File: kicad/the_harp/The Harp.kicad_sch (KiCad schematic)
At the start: 0 parts

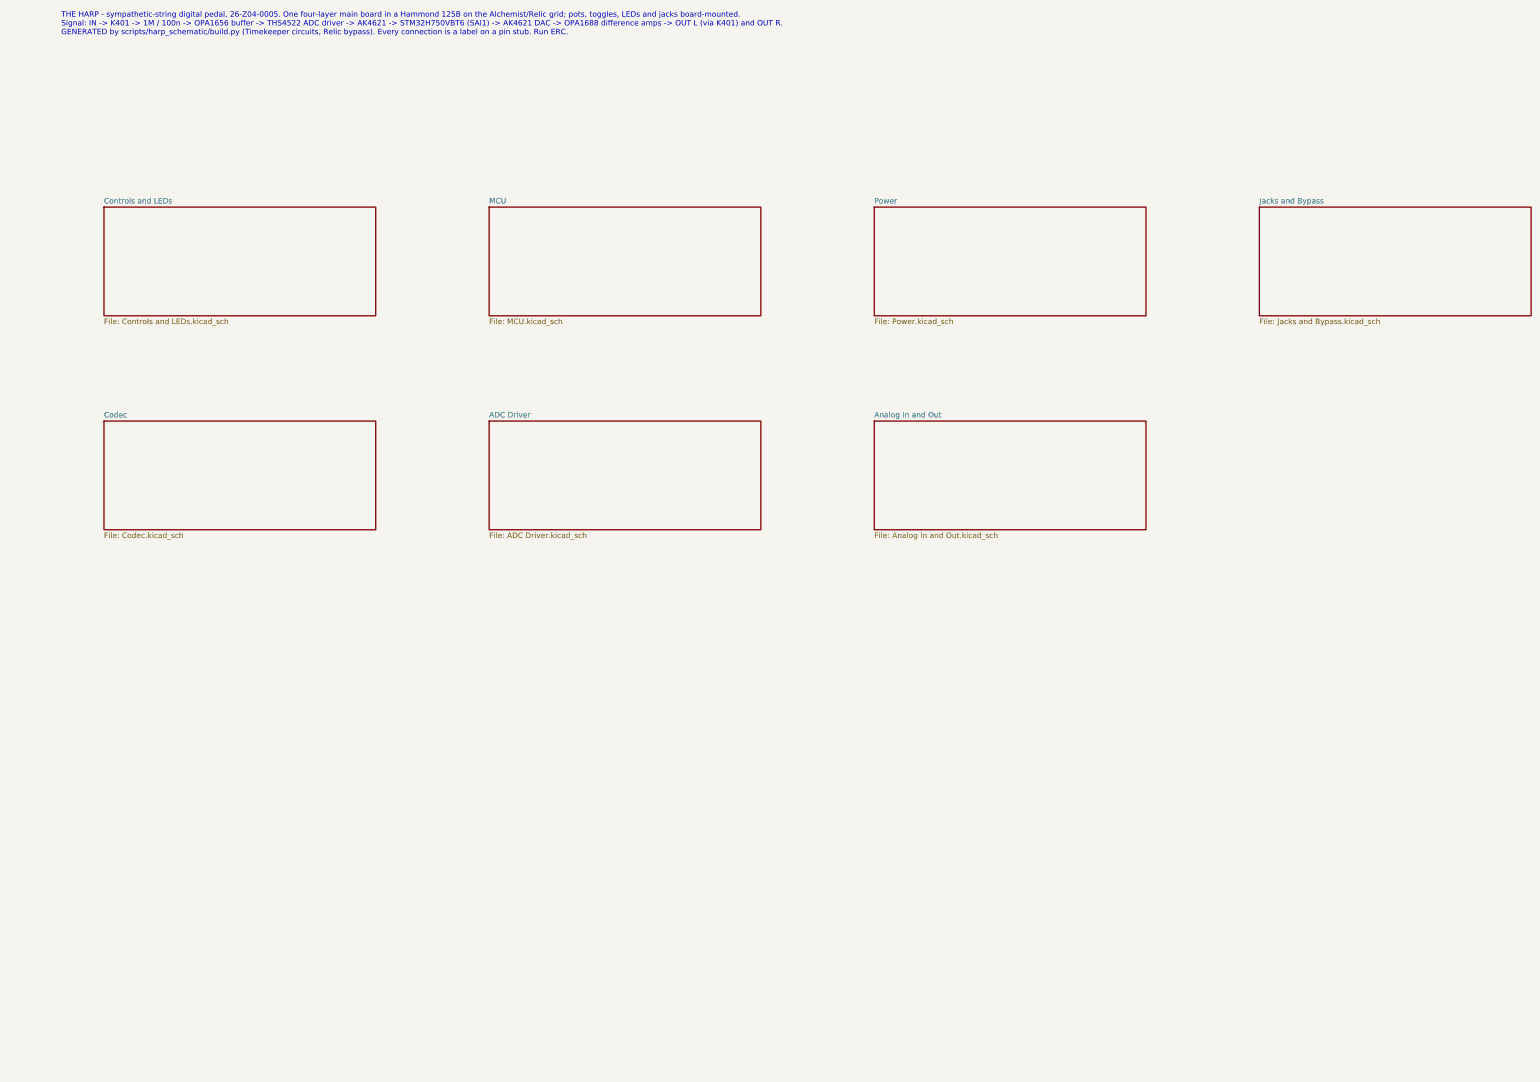
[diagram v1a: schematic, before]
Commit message: Top sheet drawn as a coloured block diagram; embed the title block and Oswald
Sheet blocks coloured by domain inside AUDIO / ANALOG, CONTROL / DIGITAL and
POWER frames, a parts summary in each block, every inter-sheet net as a
coloured arrowed line (drawing only; the sheets connect through global
labels), a legend, and the AW Titleblock 2025 worksheet and Oswald Regular /
Bold embedded as on The Relic's top sheet.

Co-Authored-By: Claude Fable 5.1 <noreply@anthropic.com>
Claude-Session: https://claude.ai/code/session_01TSLeRh1r4phcduukMUZ1ao
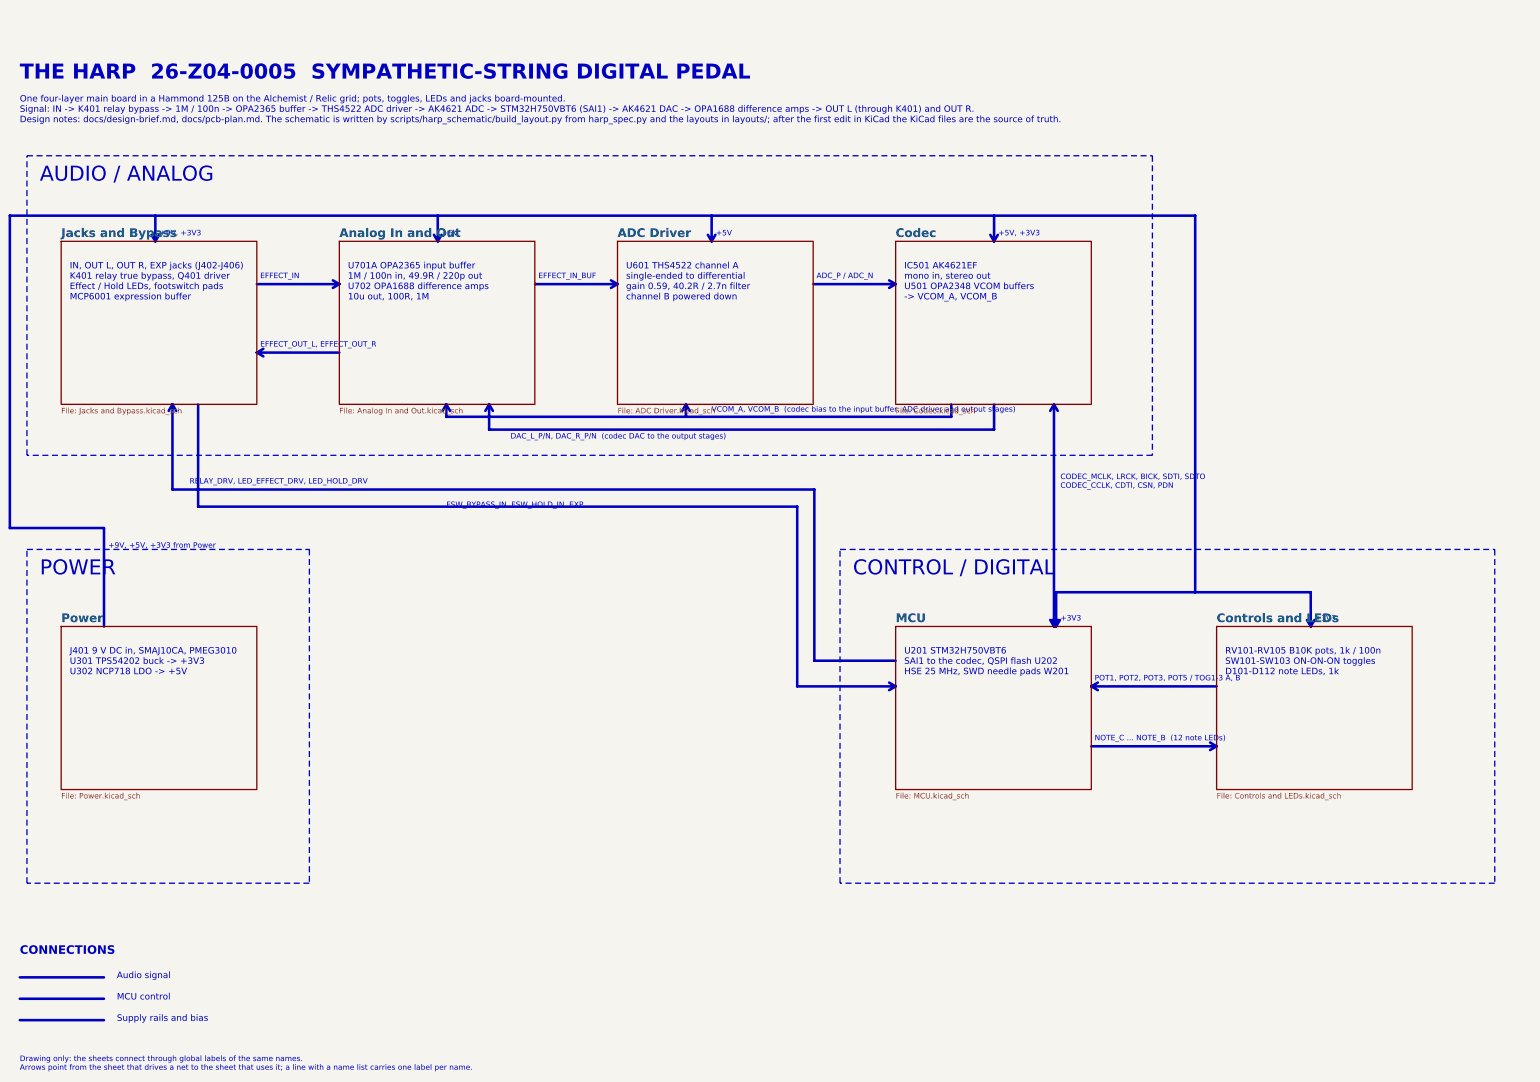
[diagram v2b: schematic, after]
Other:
- note added: "+3V3"
- note added: "+5V"
- note added: "+5V, +3V3"
- note added: "+9V, +3V3"
- note added: "+9V, +5V, +3V3 from Power"
- note added: "ADC_P / ADC_N"
- note added: "AUDIO / ANALOG"
- note added: "Audio signal"
- note added: "CODEC_MCLK, LRCK, BICK, SDTI, SDTO CODEC_CCLK, CDTI, CSN, PDN"
- note added: "CONNECTIONS"
- note added: "CONTROL / DIGITAL"
- note added: "DAC_L_P/N, DAC_R_P/N (codec DAC to the output stages)"
- note added: "Drawing only: the sheets connect through global labels of the same names. Arrows point from the sheet that drives a net to the sheet that uses it; a line with a name list carries one label per name."
- note added: "EFFECT_IN"
- note added: "EFFECT_IN_BUF"
- note added: "EFFECT_OUT_L, EFFECT_OUT_R"
- note added: "FSW_BYPASS_IN, FSW_HOLD_IN, EXP"
- note added: "IC501 AK4621EF mono in, stereo out U501 OPA2348 VCOM buffers -> VCOM_A, VCOM_B"
- note added: "IN, OUT L, OUT R, EXP jacks (J402-J406) K401 relay true bypass, Q401 driver Effect / Hold LEDs, footswitch pads MCP6001 expression buffer"
- note added: "J401 9 V DC in, SMAJ10CA, PMEG3010 U301 TPS54202 buck -> +3V3 U302 NCP718 LDO -> +5V"
- note added: "MCU control"
- note added: "NOTE_C ... NOTE_B (12 note LEDs)"
- note added: "One four-layer main board in a Hammond 125B on the Alchemist / Relic grid; pots, toggles, LEDs and jacks board-mounted. Signal: IN -> K401 relay bypass -> 1M / 100n -> OPA2365 buffer -> THS4522 ADC driver -> AK4621 ADC -> STM32H750VBT6 (SAI1) -> AK4621 DAC -> OPA1688 difference amps -> OUT L (through K401) and OUT R. Design notes: docs/design-brief.md, docs/pcb-plan.md. The schematic is written b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"
- note added: "POT1, POT2, POT3, POT5 / TOG1-3 A, B"
- note added: "POWER"
- note added: "RELAY_DRV, LED_EFFECT_DRV, LED_HOLD_DRV"
- note added: "RV101-RV105 B10K pots, 1k / 100n SW101-SW103 ON-ON-ON toggles D101-D112 note LEDs, 1k"
- note added: "Supply rails and bias"
- note added: "THE HARP 26-Z04-0005 SYMPATHETIC-STRING DIGITAL PEDAL"
- note added: "U201 STM32H750VBT6 SAI1 to the codec, QSPI flash U202 HSE 25 MHz, SWD needle pads W201"
- note added: "U601 THS4522 channel A single-ended to differential gain 0.59, 40.2R / 2.7n filter channel B powered down"
- note added: "U701A OPA2365 input buffer 1M / 100n in, 49.9R / 220p out U702 OPA1688 difference amps 10u out, 100R, 1M"
- note added: "VCOM_A, VCOM_B (codec bias to the input buffer, ADC driver and output stages)"
- note removed: "THE HARP - sympathetic-string digital pedal, 26-Z04-0005. One four-layer main board in a Hammond 125B on the Alchemist/Relic grid; pots, toggles, LEDs and jacks board-mounted. Signal: IN -> K401 -> 1M / 100n -> OPA1656 buffer -> THS4522 ADC driver -> AK4621 -> STM32H750VBT6 (SAI1) -> AK4621 DAC -> OPA1688 difference amps -> OUT L (via K401) and OUT R. GENERATED by scripts/harp_schematic/build.py 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"

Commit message: Stereo single-ended input and an OLED display
IN becomes a TRS jack (tip left, ring right) with a second OPA2365 buffer and
THS4522 channel B into the AK4621EF's AINR; the codec inputs are no longer
parked. A mono plug is detected by the right channel reading silence. The
twelve note LEDs and R107-R118 give way to a 0.91 in I2C OLED connector (J408,
PB6/PB7) with 4.7k pull-ups. Schematic regenerated (190 parts, netlist OK on
all sheets); design brief, PCB plan, firmware requirements and the design
report updated. The PCB still carries the old LED footprints until Update PCB
from Schematic is run in KiCad.

Co-Authored-By: Claude Sonnet 5.5 <noreply@anthropic.com>
Claude-Session: https://claude.ai/code/session_016hDejPHPgG8auBLMyByYZK
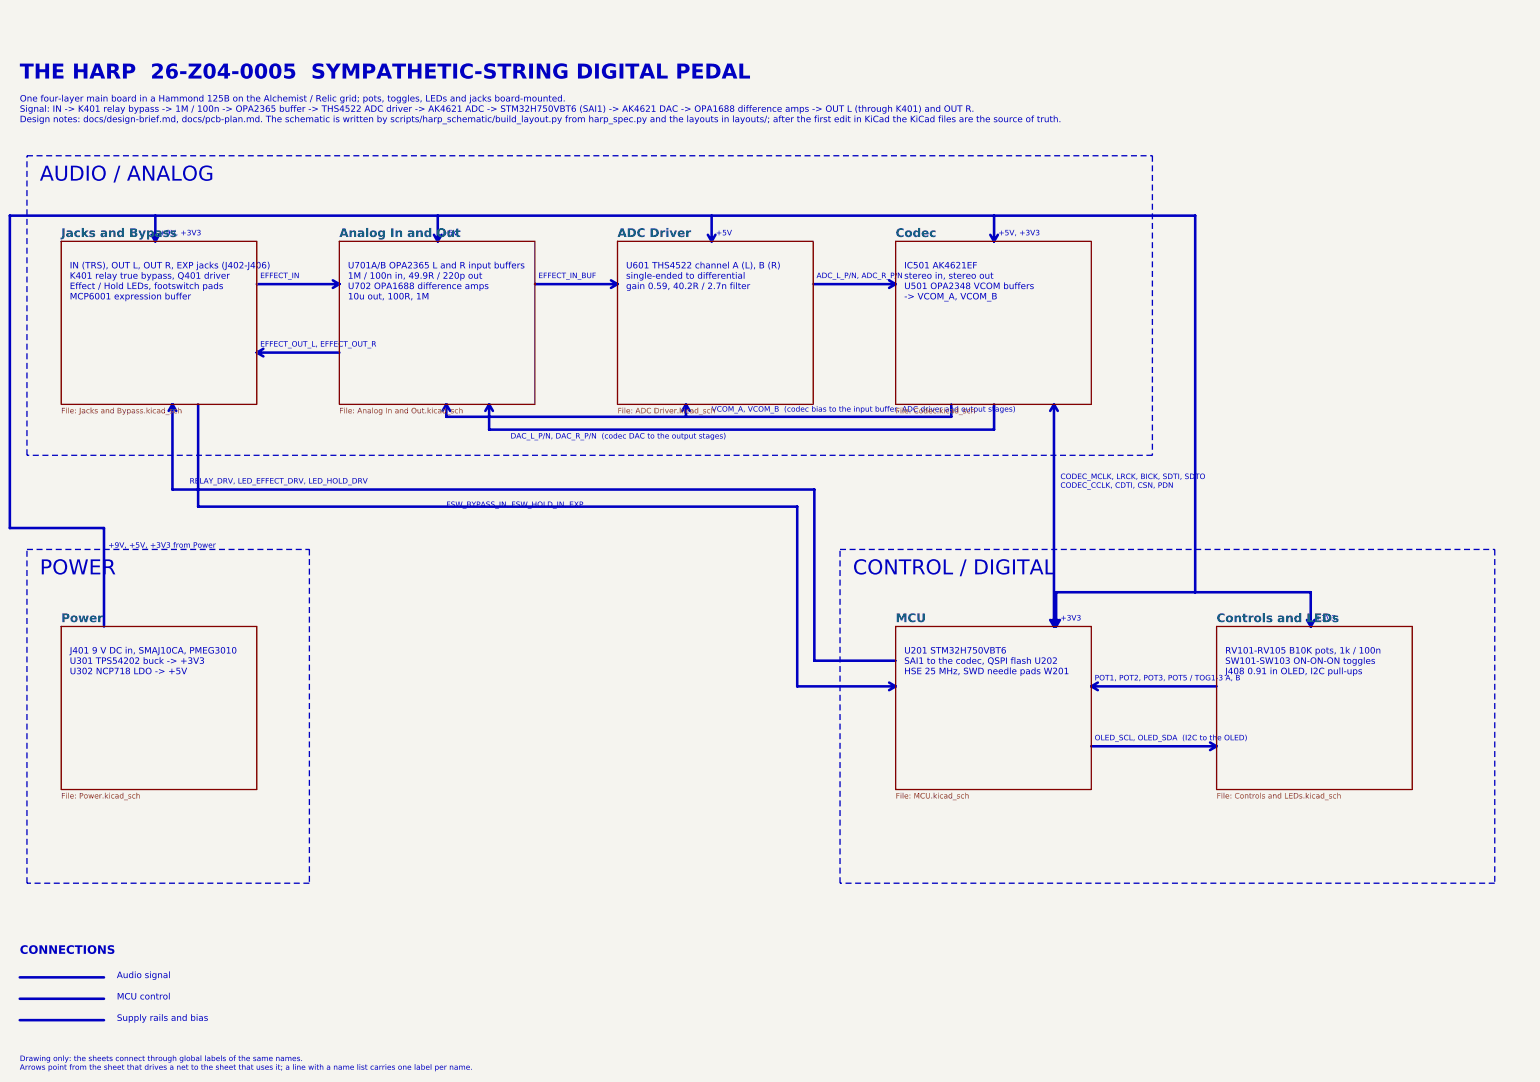
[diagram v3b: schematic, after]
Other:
- note added: "ADC_L_P/N, ADC_R_P/N"
- note added: "IC501 AK4621EF stereo in, stereo out U501 OPA2348 VCOM buffers -> VCOM_A, VCOM_B"
- note added: "IN (TRS), OUT L, OUT R, EXP jacks (J402-J406) K401 relay true bypass, Q401 driver Effect / Hold LEDs, footswitch pads MCP6001 expression buffer"
- note added: "OLED_SCL, OLED_SDA (I2C to the OLED)"
- note added: "RV101-RV105 B10K pots, 1k / 100n SW101-SW103 ON-ON-ON toggles J408 0.91 in OLED, I2C pull-ups"
- note added: "U601 THS4522 channel A (L), B (R) single-ended to differential gain 0.59, 40.2R / 2.7n filter"
- note added: "U701A/B OPA2365 L and R input buffers 1M / 100n in, 49.9R / 220p out U702 OPA1688 difference amps 10u out, 100R, 1M"
- note removed: "ADC_P / ADC_N"
- note removed: "IC501 AK4621EF mono in, stereo out U501 OPA2348 VCOM buffers -> VCOM_A, VCOM_B"
- note removed: "IN, OUT L, OUT R, EXP jacks (J402-J406) K401 relay true bypass, Q401 driver Effect / Hold LEDs, footswitch pads MCP6001 expression buffer"
- note removed: "NOTE_C ... NOTE_B (12 note LEDs)"
- note removed: "RV101-RV105 B10K pots, 1k / 100n SW101-SW103 ON-ON-ON toggles D101-D112 note LEDs, 1k"
- note removed: "U601 THS4522 channel A single-ended to differential gain 0.59, 40.2R / 2.7n filter channel B powered down"
- note removed: "U701A OPA2365 input buffer 1M / 100n in, 49.9R / 220p out U702 OPA1688 difference amps 10u out, 100R, 1M"
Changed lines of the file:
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@@
 		)
 	)
-	(text "IN, OUT L, OUT R, EXP jacks (J402-J406)\nK401 relay true bypass, Q401 driver\nEffect / Hold LEDs, footswitch pads\nMCP6001 expression buffer"
+	(text "IN (TRS), OUT L, OUT R, EXP jacks (J402-J406)\nK401 relay true bypass, Q401 driver\nEffect / Hold LEDs, footswitch pads\nMCP6001 expression buffer"
 		(exclude_from_sim no)
 		(at 32 83 0)
@@
 		)
 	)
-	(text "U701A OPA2365 input buffer\n1M / 100n in, 49.9R / 220p out\nU702 OPA1688 difference amps\n10u out, 100R, 1M"
+	(text "U701A/B OPA2365 L and R input buffers\n1M / 100n in, 49.9R / 220p out\nU702 OPA1688 difference amps\n10u out, 100R, 1M"
 		(exclude_from_sim no)
 		(at 97 83 0)
@@
 		)
 	)
-	(text "U601 THS4522 channel A\nsingle-ended to differential\ngain 0.59, 40.2R / 2.7n filter\nchannel B powered down"
+	(text "U601 THS4522 channel A (L), B (R)\nsingle-ended to differential\ngain 0.59, 40.2R / 2.7n filter"
 		(exclude_from_sim no)
 		(at 162 83 0)
@@
 		)
 	)
-	(text "IC501 AK4621EF\nmono in, stereo out\nU501 OPA2348 VCOM buffers\n-> VCOM_A, VCOM_B"
+	(text "IC501 AK4621EF\nstereo in, stereo out\nU501 OPA2348 VCOM buffers\n-> VCOM_A, VCOM_B"
 		(exclude_from_sim no)
 		(at 227 83 0)
@@
 		)
 	)
-	(text "RV101-RV105 B10K pots, 1k / 100n\nSW101-SW103 ON-ON-ON toggles\nD101-D112 note LEDs, 1k"
+	(text "RV101-RV105 B10K pots, 1k / 100n\nSW101-SW103 ON-ON-ON toggles\nJ408 0.91 in OLED, I2C pull-ups"
 		(exclude_from_sim no)
 		(at 302 173 0)
@@
 		)
 	)
-	(text "ADC_P / ADC_N"
+	(text "ADC_L_P/N, ADC_R_P/N"
 		(exclude_from_sim no)
 		(at 206.5 87 0)
@@
 		)
 	)
-	(text "NOTE_C ... NOTE_B  (12 note LEDs)"
+	(text "OLED_SCL, OLED_SDA  (I2C to the OLED)"
 		(exclude_from_sim no)
 		(at 271.5 195 0)
